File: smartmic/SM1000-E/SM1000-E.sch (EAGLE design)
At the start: 198 parts, among them CN1 HDR100-3, CN10 ST-3509, CN11 HDR100-3, CN12 HRS-A3C-16DA, CN2 JS-MU3-002, CN3 DS-0518, CN4 RJ-45, CN5 ST-3509, CN6 ST-3509, CN7 ST-3509, CN8 ST-3509, CN9 ST-3509, J1 JMP-2PIN, J2 JMP-2PIN, J3 JMP-2PIN, J4 CONN-BOOM-XH-2A, P1 TPAD50, P10 TPAD50, P11 TPAD50, P12 TPAD50, P13 TPAD50, P14 TPAD50, P16 TPAD50, P18 TPAD50, P19 TPAD50, P2 TPAD50, P20 TPAD50, P3 TPAD50, P4 TPAD50, P5 TPAD50, P6 TPAD50, P7 TPAD50, P8 TPAD50, P9 TPAD50, SW1 SW-LC2259, SW2 TS-026, SW3 SW-LC2259EENP, SW4 TS-026, SW5 TS-02B, T1 SM-LP-5001, T2 SM-LP-5001, U1 STM32F405VGT6, U2 LD3985M33R, U3 STMPS2141, U4 EMIF02-USB03F2, U5 TPS54329E, U6 LMV341, U7 LMV341, U8 LM386M-1, U9 LMV341

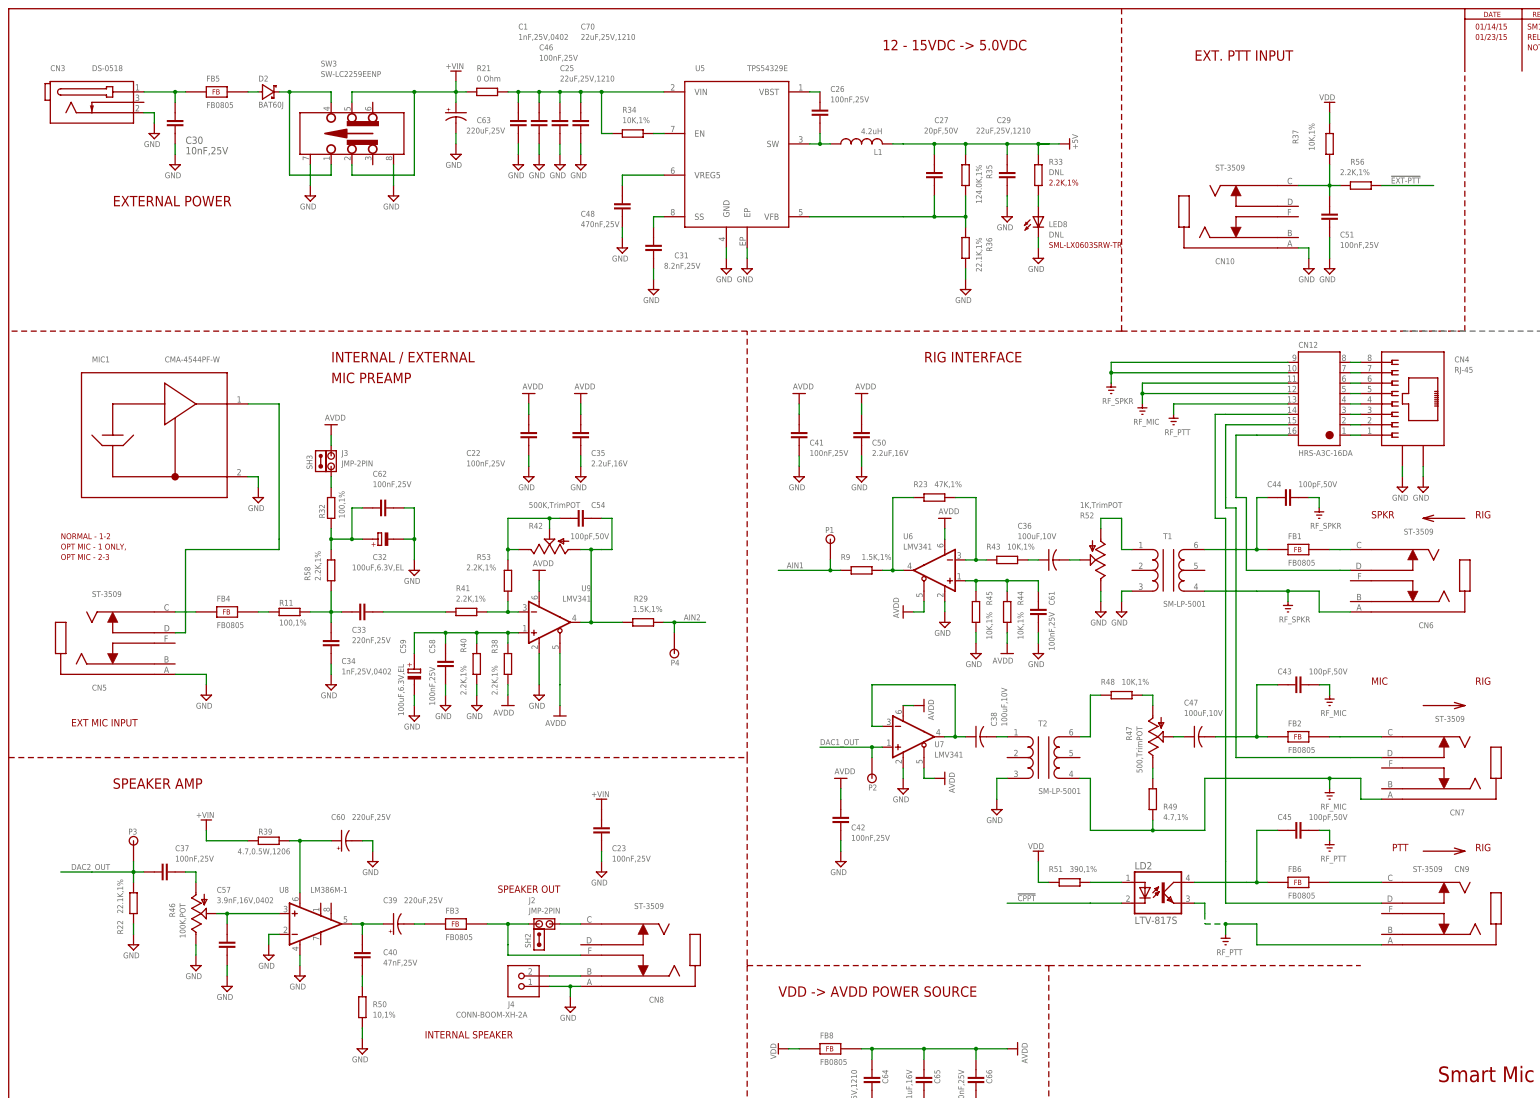
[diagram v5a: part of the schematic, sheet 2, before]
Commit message: 
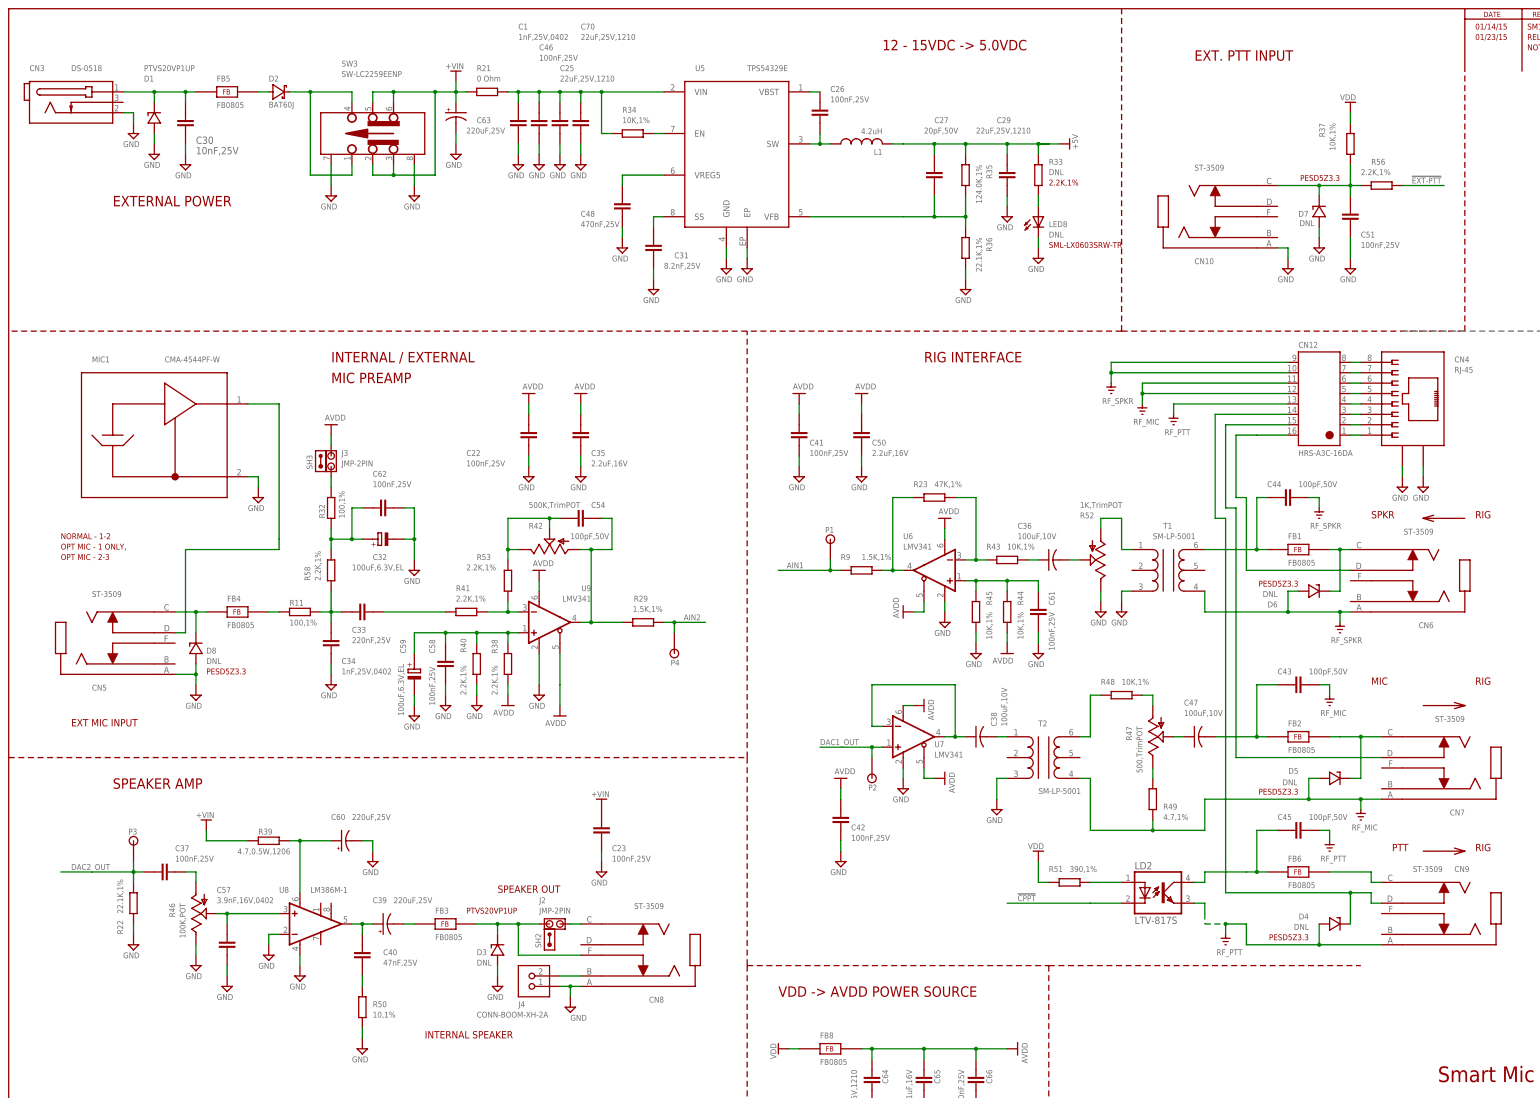
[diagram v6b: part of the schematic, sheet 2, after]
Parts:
- added D1: PTVS20VP1UP, _RoweTel:PTVS20VP1UP
- added D3: DNL, _RoweTel:PTVS20VP1UP
- added D4, D5, D6, D7, D8: DNL, _RoweTel:PESD5ZX
- LED5: value SML-LX0603SRW -> DNL
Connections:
- removed net N$64: CN6.C, FB1.2
- new net N$84: CN6.C, D6.C, FB1.2
- net +VIN: now also SW3.3, SW3.6
- net APTT: now also D4.C
- net GND: now also D1.A, D3.A, D7.A, D8.A
- net N$15: now also D7.C
- net N$62: now also D3.C
- net N$70: now also D5.C
- net N$76: now also D8.C
- net N$77: now also D1.C
- net RF_MIC: now also D5.A
- net RF_PTT: now also D4.A
- net RF_SPKR: now also D6.A
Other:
- note added: "06/01/15"
- note added: "ADD D1,D3,D4,D5,D6,D7,D8 TSV"
- note added: "PESD5Z3.3"
- note added: "PTVS20VP1UP"
- moved on the sheet: C30, C39, C51, CN10, CN3, D2, FB3, FB4, FB5, FB6, J2, J4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
